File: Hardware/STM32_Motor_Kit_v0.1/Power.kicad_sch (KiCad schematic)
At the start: 66 parts, among them J1 Conn_01x02_Male, U2 AMS111733TR-HT, U3 LMV358IDRG4, U4 TPS54331DR, U5 MC78M15CDTRKG-

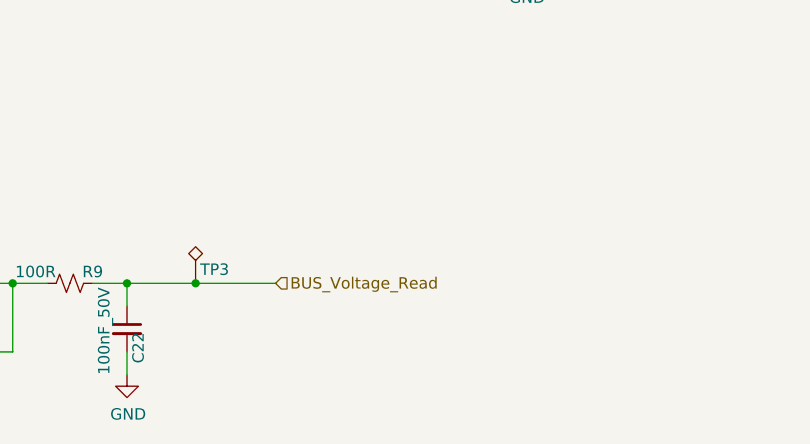
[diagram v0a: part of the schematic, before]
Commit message: Firmware Configuration added, Motor Control Pins and BackEMF Analog Pins setted.
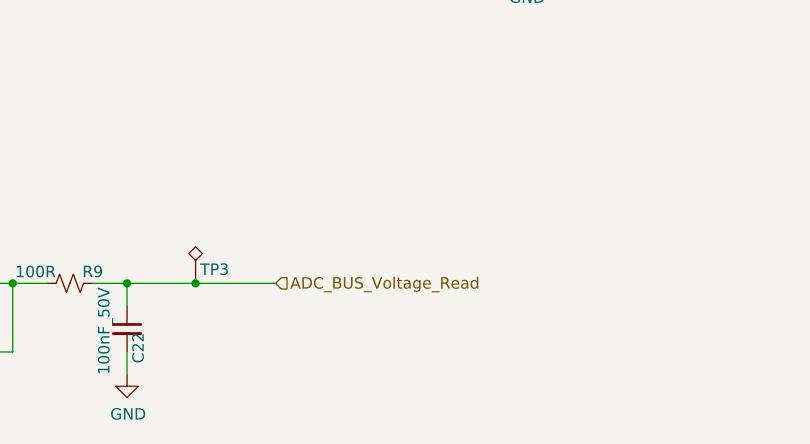
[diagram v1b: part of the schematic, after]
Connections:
- net BUS_Voltage_Read renamed ADC_BUS_Voltage_Read
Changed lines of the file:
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@@
 		)
 	)
-	(hierarchical_label "BUS_Voltage_Read"
+	(hierarchical_label "ADC_BUS_Voltage_Read"
 		(shape input)
 		(at 151.13 168.91 0)

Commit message: 23.08.2024
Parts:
- R6: value 1K -> 10K
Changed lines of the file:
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@@
 			)
 		)
-		(property "Value" "1K"
+		(property "Value" "10K"
 			(at 68.58 49.53 90)
 			(effects

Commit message: 16.09.2024
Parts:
- removed C103: 220uF_50V, AKE_Capacitor_TH:CP_Radial_D10.0mm_P5.00mm, symbol AKE_Capacitor:Capacitor_Polarised
- added D31: 10V, AKE_Diode_SMD:SMA, symbol AKE_Diode:Diode_Zener
- added Q8: PJD35P03_L2_00001, AKE_Mosfet_SMD:DPAK_123, symbol AKE_MOSFET:PJD35P03_L2_00001
- added R73: 100K, AKE_Resistor_SMD:RES_1206, symbol AKE_Resistor:Resistor_US
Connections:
- net GND: now also R73.1
- net Vbus: now also D31.1, Q8.3 (S); no longer D1.1, F1.2, L1.1
- new net: D31.2, Q8.1 (G), R73.2
- new net: D1.1, F1.2, L1.1, Q8.2 (D)
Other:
- note added: "Motor VBUS"
- moved on the sheet: C19, C21, C24, C25, C28, C30, C31, C32, C33, C34, D1, D2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

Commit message: 12.01.2025
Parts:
- added C121: 100nF_50V, AKE_Capacitor_SMD:CAP_0603, symbol AKE_Capacitor:Capacitor_UnPolarised
- added C122: 100pF_50V, AKE_Capacitor_SMD:CAP_0603, symbol AKE_Capacitor:Capacitor_UnPolarised
- added L7: 180nH, AKE_Inductor_SMD:IND_0603, symbol AKE_Inductor:Inductor
- added R129: 14.7K, AKE_Resistor_SMD:RES_0603, symbol AKE_Resistor:Resistor_US
- added R130: 33.2K, AKE_Resistor_SMD:RES_0603, symbol AKE_Resistor:Resistor_US
- C110: value 1uF_10V -> 1nF_50V
- C17: value 100nF_50V -> 1.2nF_50V
- C22: value 100nF_50V -> 10nF_50V
- R7: value 100R -> 8.45K
- R9: value 100R -> 787R
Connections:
- net GND: now also C121.2, C122.2; no longer C110.2
- net at R9.2, U3.6 (-), U3.7: now also C110.2
- net at C15.1, JP3.1 (A): now also L7.1; no longer C110.1, U3.8 (V+)
- net at C17.1, R7.1: now also R129.2; no longer U3.5 (+)
- new net: C121.1, L7.2, U3.8 (V+)
- new net: C110.1, R129.1, R130.2
- new net: C122.1, R130.1, U3.5 (+)
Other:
- note added: "OK"
- moved on the sheet: C13, C15, C22, JP3, R3, R4, R5, R9, TP3, U3B
